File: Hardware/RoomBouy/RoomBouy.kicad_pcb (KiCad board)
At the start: 2 copper layers, 65 x 56.5 mm, 1 part, among them J2 Raspberry_Pi_2_3

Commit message: Clean sheet
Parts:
- moved J2 174.3 mm to (0.16, -24.8)
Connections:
- net Net-(J2-GND-Pad14) renamed GND
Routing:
- added copper zone on B.Cu, net GND
- added copper zone on F.Cu, net GND
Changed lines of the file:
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@@
 	(net 1 "unconnected-(J2-GPIO26-Pad37)")
 	(net 2 "Net-(J2-5V-Pad2)")
-	(net 3 "Net-(J2-GND-Pad14)")
+	(net 3 "GND")
 	(net 4 "unconnected-(J2-~{CE1}{slash}GPIO7-Pad26)")
 	(net 5 "unconnected-(J2-GPIO23-Pad16)")
@@
 	(footprint "RPI_Hat:RPI_Hat_B+"
 		(layer "F.Cu")
-		(at 144.24 73.222)
+		(at 0.16 -24.838)
 		(property "Reference" "J2"
 			(at 23.5 3.5 0)
@@
 			(layer "Dwgs.User")
 			(pts
-				(xy 115.24 126.722) (xy 111.74 126.722)
+				(xy -28.84 28.662) (xy -32.34 28.662)
 			)
 			(height -2.5)
 			(gr_text "3.5000 mm"
-				(at 113.49 127.572 0)
+				(at -30.59 29.512 0)
 				(layer "Dwgs.User")
 				(effects
@@
 			(layer "Dwgs.User")
 			(pts
-				(xy 158.74 122.722) (xy 158.74 105.722)
+				(xy 14.66 24.662) (xy 14.66 7.662)
 			)
 			(height 3)
 			(gr_text "17.0000 mm"
-				(at 160.09 114.222 90)
+				(at 16.01 16.162 90)
 				(layer "Dwgs.User")
 				(effects
@@
 			(layer "Dwgs.User")
 			(pts
-				(xy 154.74 125.722) (xy 154.74 114.222)
+				(xy 10.66 27.662) (xy 10.66 16.162)
 			)
 			(height -2.499999)
 			(gr_text "11.5000 mm"
-				(at 150.590001 119.972 90)
+				(at 6.510001 21.912 90)
 				(layer "Dwgs.User")
 				(effects
@@
 			(layer "Dwgs.User")
 			(pts
-				(xy 176.74 68.222) (xy 111.74 68.222)
+				(xy 32.66 -29.838) (xy -32.34 -29.838)
 			)
 			(height 7)
 			(gr_text "65.0000 mm"
-				(at 144.24 59.572 0)
+				(at 0.16 -38.488 0)
 				(layer "Dwgs.User")
 				(effects
@@
 			(layer "Dwgs.User")
 			(pts
-				(xy 110.74 125.722) (xy 110.74 106.222)
+				(xy -33.34 27.662) (xy -33.34 8.162)
 			)
 			(height -3)
 			(gr_text "19.5000 mm"
-				(at 106.09 115.972 90)
+				(at -37.99 17.912 90)
 				(layer "Dwgs.User")
 				(effects
@@
 			(layer "Dwgs.User")
 			(pts
-				(xy 177.74 125.722) (xy 177.74 69.722)
+				(xy 33.66 27.662) (xy 33.66 -28.338)
 			)
 			(height 8)
 			(gr_text "56.0000 mm"
-				(at 184.09 97.722 90)
+				(at 40.01 -0.338 90)
 				(layer "Dwgs.User")
 				(effects
@@
 			(layer "Dwgs.User")
 			(pts
-				(xy 157.74 104.722) (xy 155.74 104.722)
+				(xy 13.66 6.662) (xy 11.66 6.662)
 			)
 			(height 2.499999)
 			(gr_text "2.0000 mm"
-				(at 156.74 100.572001 0)
+				(at 12.66 2.512001 0)
 				(layer "Dwgs.User")
 				(effects
@@
 			(layer "Dwgs.User")
 			(pts
-				(xy 173.24 68.222) (xy 115.24 68.222)
+				(xy 29.16 -29.838) (xy -28.84 -29.838)
 			)
 			(height 2.5)
 			(gr_text "58.0000 mm"
-				(at 144.24 64.072 0)
+				(at 0.16 -33.988 0)
 				(layer "Dwgs.User")
 				(effects
@@
 			(layer "Dwgs.User")
 			(pts
-				(xy 177.74 122.222) (xy 177.74 73.222)
+				(xy 33.66 24.162) (xy 33.66 -24.838)
 			)
 			(height 2.999999)
 			(gr_text "49.0000 mm"
-				(at 179.089999 97.722 90)
+				(at 35.009999 -0.338 90)
 				(layer "Dwgs.User")
 				(effects
@@
 			(layer "Dwgs.User")
 			(pts
-				(xy 177.74 125.722) (xy 177.74 69.222)
+				(xy 33.66 27.662) (xy 33.66 -28.838)
 			)
 			(height 12)
 			(gr_text "56.5000 mm"
-				(at 188.09 97.472 90)
+				(at 44.01 -0.588 90)
 				(layer "Dwgs.User")
 				(effects
@@
 			(layer "Dwgs.User")
 			(pts
-				(xy 116.74 89.222) (xy 111.74 89.222)
+				(xy -27.34 -8.838) (xy -32.34 -8.838)
 			)
 			(height 2)
 			(gr_text "5.0000 mm"
-				(at 114.24 85.572 0)
+				(at -29.84 -12.488 0)
 				(layer "Dwgs.User")
 				(effects
@@
 			(layer "Dwgs.User")
 			(pts
-				(xy 118.74 125.722) (xy 118.74 122.222)
+				(xy -25.34 27.662) (xy -25.34 24.162)
 			)
 			(height 3)
 			(gr_text "3.5000 mm"
-				(at 120.09 123.972 90)
+				(at -23.99 25.912 90)
 				(layer "Dwgs.User")
 				(effects
@@
 			(layer "Dwgs.User")
 			(pts
-				(xy 144.24 75.222001) (xy 115.24 75.222001)
+				(xy 0.16 -22.837999) (xy -28.84 -22.837999)
 			)
 			(height -2.499999)
 			(gr_text "29.0000 mm"
-				(at 129.74 79.722001 0)
+				(at -14.34 -18.337999 0)
 				(layer "Dwgs.User")
 				(effects
@@
 			(layer "Dwgs.User")
 			(pts
-				(xy 117.74 106.222) (xy 117.74 89.222)
+				(xy -26.34 8.162) (xy -26.34 -8.838)
 			)
 			(height 2)
 			(gr_text "17.0000 mm"
-				(at 118.09 97.722 90)
+				(at -25.99 -0.338 90)
 				(layer "Dwgs.User")
 				(effects
@@
 			(layers "*.Cu" "*.Mask")
 			(remove_unused_layers no)
-			(net 3 "Net-(J2-GND-Pad14)")
+			(net 3 "GND")
 			(pinfunction "GND")
 			(pintype "power_in")
@@
 			(layers "*.Cu" "*.Mask")
 			(remove_unused_layers no)
-			(net 3 "Net-(J2-GND-Pad14)")
+			(net 3 "GND")
 			(pinfunction "GND")
 			(pintype "passive")
@@
 			(layers "*.Cu" "*.Mask")
 			(remove_unused_layers no)
-			(net 3 "Net-(J2-GND-Pad14)")
+			(net 3 "GND")
 			(pinfunction "GND")
 			(pintype "passive")
@@
 			(layers "*.Cu" "*.Mask")
 			(remove_unused_layers no)
-			(net 3 "Net-(J2-GND-Pad14)")
+			(net 3 "GND")
 			(pinfunction "GND")
 			(pintype "passive")
@@
 			(layers "*.Cu" "*.Mask")
 			(remove_unused_layers no)
-			(net 3 "Net-(J2-GND-Pad14)")
+			(net 3 "GND")
 			(pinfunction "GND")
 			(pintype "passive")
@@
 			(layers "*.Cu" "*.Mask")
 			(remove_unused_layers no)
-			(net 3 "Net-(J2-GND-Pad14)")
+			(net 3 "GND")
 			(pinfunction "GND")
 			(pintype "passive")
@@
 			(layers "*.Cu" "*.Mask")
 			(remove_unused_layers no)
-			(net 3 "Net-(J2-GND-Pad14)")
+			(net 3 "GND")
 			(pinfunction "GND")
 			(pintype "passive")
@@
 			(layers "*.Cu" "*.Mask")
 			(remove_unused_layers no)
-			(net 3 "Net-(J2-GND-Pad14)")
+			(net 3 "GND")
 			(pinfunction "GND")
 			(pintype "passive")
@@
 		)
 	)
+	(zone
+		(net 3)
+		(net_name "GND")
+		(layers "F&B.Cu")
+		(hatch edge 0.5)
+		(connect_pads
+			(clearance 0.5)
+		)
+		(min_thickness 0.25)
+		(filled_areas_thickness no)
+		(fill yes
+			(thermal_gap 0.5)
+			(thermal_bridge_width 0.5)
+		)
+		(polygon
+			(pts
+				(xy 32.92 -29.06) (xy 32.92 27.94) (xy -33.08 27.94) (xy -33.08 -29.06)
+			)
+		)
+	)

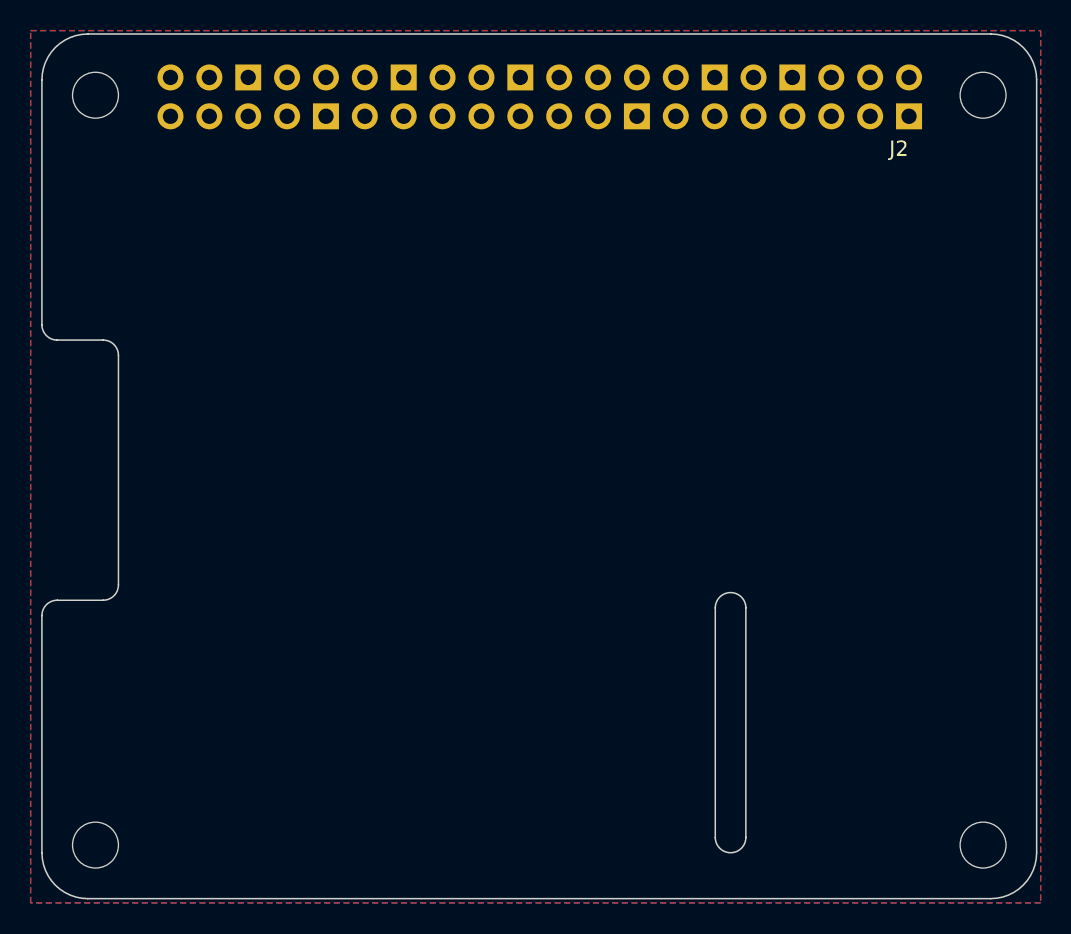
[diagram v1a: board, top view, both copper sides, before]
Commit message: Add internal libs, do full board layout, bump k8 and fix ERC
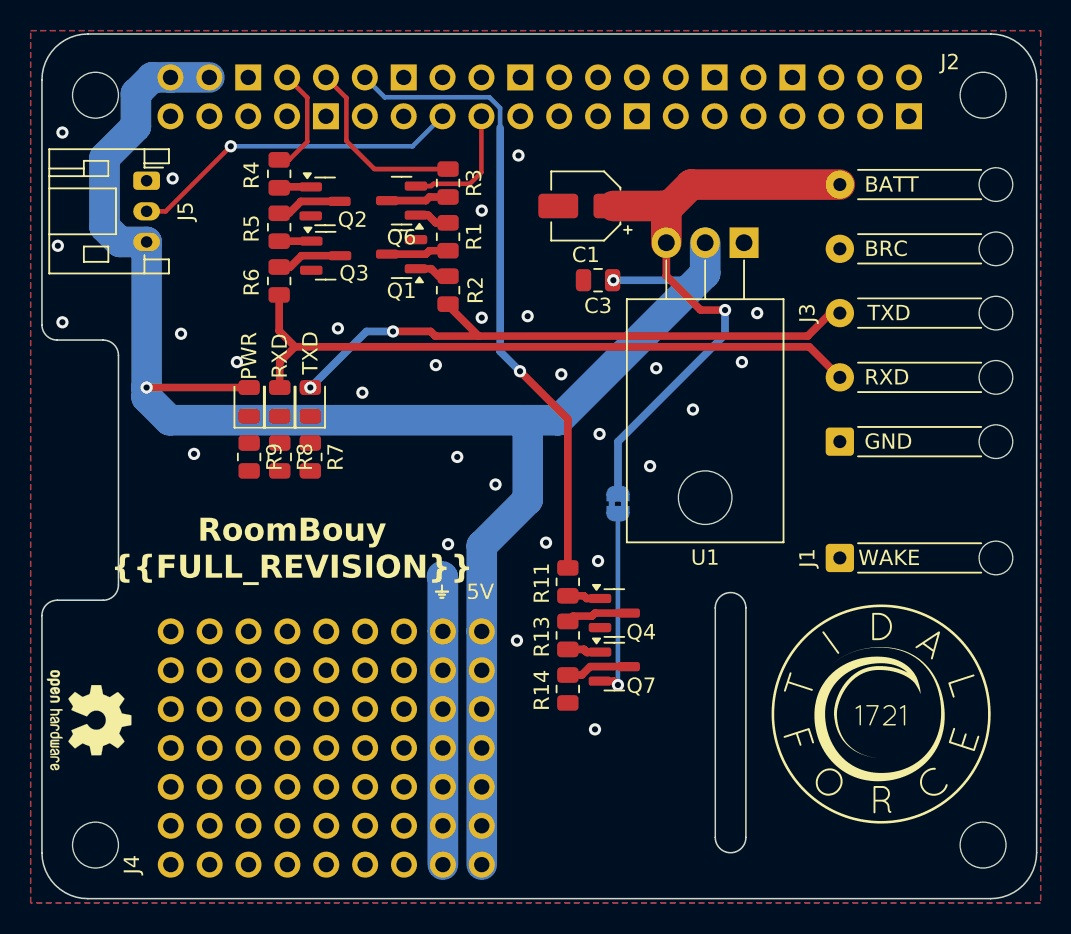
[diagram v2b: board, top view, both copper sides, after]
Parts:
- added C1: 10uf, Capacitor_SMD:CP_Elec_4x3, F.Cu at (3.20, -17.6)
- added C3: 1uF, Capacitor_SMD:C_0805_2012Metric, F.Cu at (4.00, -12.8)
- added D1: TXD, LED_SMD:LED_0805_2012Metric, F.Cu at (-14.8, -4.80)
- added D2: RXD, LED_SMD:LED_0805_2012Metric, F.Cu at (-16.8, -4.80)
- added D3: PWR, LED_SMD:LED_0805_2012Metric, F.Cu at (-18.8, -4.80)
- added G***: LOGO, KenwoodFox:TIDAL_FORCE_LOGO, F.Cu at (22.5, 15.6)
- added G***: LOGO, KenwoodFox:KITSUNE_LOGO, B.Cu at (21.0, 15.8)
- added J1: Roomba Wake, Connector_Wire:SolderWire-0.25sqmm_1x01_D0.65mm_OD1.7mm_Relief, F.Cu at (19.8, 5.40)
- added J3: Roomba Connector, Connector_Wire:SolderWire-0.25sqmm_1x05_P4.2mm_D0.65mm_OD1.7mm_Relief, F.Cu at (19.8, -2.20)
- added J4: ProtoPad, RoomBouy:ProtoPad, F.Cu at (-13.8, 17.8)
- added J5: Servo, Connector_JST:JST_PH_S3B-PH-K_1x03_P2.00mm_Horizontal, F.Cu at (-25.5, -19.2)
- added JP1: SolderJumper_2_Bridged, Jumper:SolderJumper-2_P1.3mm_Bridged2Bar_RoundedPad1.0x1.5mm, B.Cu at (5.30, 1.85)
- added Q1: MMBT3904, Package_TO_SOT_SMD:SOT-23, F.Cu at (-8.84, -14.4)
- added Q2: MMBT3904, Package_TO_SOT_SMD:SOT-23, F.Cu at (-13.8, -17.9)
- added Q3: MMBT3906, Package_TO_SOT_SMD:SOT-23, F.Cu at (-13.8, -14.3)
- added Q4: MMBT3904, Package_TO_SOT_SMD:SOT-23, F.Cu at (5.06, 9.00)
- added Q6: MMBT3906, Package_TO_SOT_SMD:SOT-23, F.Cu at (-8.84, -17.9)
- added Q7: MMBT3906, Package_TO_SOT_SMD:SOT-23, F.Cu at (5.06, 12.5)
- added R1: 1k, Resistor_SMD:R_0805_2012Metric, F.Cu at (-5.80, -15.6)
- added R11: 1k, Resistor_SMD:R_0805_2012Metric, F.Cu at (2.02, 6.96)
- added R13: 1k, Resistor_SMD:R_0805_2012Metric, F.Cu at (2.02, 10.5)
- added R14: 1k, Resistor_SMD:R_0805_2012Metric, F.Cu at (2.02, 14.0)
- added R2: 1k, Resistor_SMD:R_0805_2012Metric, F.Cu at (-5.80, -12.1)
- added R3: 1k, Resistor_SMD:R_0805_2012Metric, F.Cu at (-5.80, -19.1)
- added R4: 1k, Resistor_SMD:R_0805_2012Metric, F.Cu at (-16.8, -19.7)
- added R5: 1k, Resistor_SMD:R_0805_2012Metric, F.Cu at (-16.8, -16.2)
- added R6: 1k, Resistor_SMD:R_0805_2012Metric, F.Cu at (-16.8, -12.7)
- added R7: 1k, Resistor_SMD:R_0805_2012Metric, F.Cu at (-14.8, -1.20)
- added R8: 1k, Resistor_SMD:R_0805_2012Metric, F.Cu at (-16.8, -1.20)
- added R9: 1k, Resistor_SMD:R_0805_2012Metric, F.Cu at (-18.8, -1.20)
- added REF**: OSHW-Logo2_7.3x6mm_SilkScreen, Symbol:OSHW-Logo2_7.3x6mm_SilkScreen, F.Cu at (-29.2, 16.0)
- added REF**: KiCad-Logo2_5mm_SilkScreen, Symbol:KiCad-Logo2_5mm_SilkScreen, B.Cu at (20.8, 23.8)
- added U1: LM1084-5.0, Package_TO_SOT_THT:TO-220-3_Horizontal_TabDown, F.Cu at (13.5, -15.2)
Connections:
- net Net-(J2-3V3-Pad1) renamed +3.3V
- net Net-(J2-5V-Pad2) renamed +5V
- J2 pad 10: unconnected-(J2-GPIO15/RXD-Pad10) -> /PI_RXD
- J2 pad 12: unconnected-(J2-GPIO18/PWM0-Pad12) -> /GPIO18
- J2 pad 15: unconnected-(J2-GPIO22-Pad15) -> /SERVO
- J2 pad 8: unconnected-(J2-GPIO14/TXD-Pad8) -> /PI_TXD
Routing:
- net +5V: track 0.00 -> 114.4 mm, vias 0 -> 2
- net /ROOMBA_RXD: track 0.00 -> 43.3 mm
- net /GPIO18: track 0.00 -> 41.6 mm, vias 0 -> 1
- net /ROOMBA_TXD: track 0.00 -> 39.8 mm, vias 0 -> 2
- net +BATT: track 0.00 -> 39.6 mm, vias 0 -> 1
- net /SERVO: track 0.00 -> 21.9 mm, vias 0 -> 1
- net GND: track 0.00 -> 18.9 mm, vias 0 -> 28
- net Net-(JP1-A): track 0.00 -> 12.5 mm, vias 0 -> 1
- net /PI_RXD: track 0.00 -> 12.1 mm
- net +3.3V: track 0.00 -> 8.31 mm
- net /PI_TXD: track 0.00 -> 7.08 mm
- net Net-(Q3-C): track 0.00 -> 4.28 mm
- net Net-(Q2-C): track 0.00 -> 4.26 mm
- net Net-(Q7-C): track 0.00 -> 4.20 mm
- net Net-(Q4-C): track 0.00 -> 4.20 mm
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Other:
- board text added: "5V"
- board text added: "BATT"
- board text added: "BRC"
- board text added: "GND"
- board text added: "RXD"
- board text added: "RoomBouy {{FULL_REVISION}}"
- board text added: "TXD"
- board text added: "WAKE"
- board text added: "{dblquote}Societies get the best of what they celebrate.{dblquote} -Woodie Flowers"

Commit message: Fix DRC
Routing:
- net /ROOMBA_WAKE: track 0.00 -> 23.7 mm
- net +5V: track 114.4 -> 125.5 mm, vias 2 -> 3
- net Net-(D3-K): track 0.00 -> 1.75 mm
- net Net-(D2-K): track 0.00 -> 1.75 mm
- net Net-(D1-K): track 0.00 -> 1.75 mm
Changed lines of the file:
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@@
 		(tags "SOT TO_SOT_SMD")
 		(property "Reference" "Q4"
-			(at 1.7625 1.25 360)
+			(at 1.7625 1.25 0)
 			(layer "F.SilkS")
 			(effects
@@
 		)
 		(property "Value" "MMBT3904"
-			(at 0 2.4 360)
+			(at 0 2.4 0)
 			(layer "F.Fab")
 			(effects
@@
 		)
 		(fp_text user "${REFERENCE}"
-			(at 0 0 360)
+			(at 0 0 0)
 			(layer "F.Fab")
 			(effects
@@
 		(tags "resistor")
 		(property "Reference" "R8"
-			(at 0 -1.65 90)
+			(at 2.7 -0.05 90)
 			(layer "F.SilkS")
 			(effects
@@
 		(tags "SOT TO_SOT_SMD")
 		(property "Reference" "Q2"
-			(at 1.8 1.2 360)
+			(at 1.8 1.2 0)
 			(layer "F.SilkS")
 			(effects
@@
 		)
 		(property "Value" "MMBT3904"
-			(at 0 2.4 360)
+			(at 0 2.4 0)
 			(layer "F.Fab")
 			(effects
@@
 		)
 		(fp_text user "${REFERENCE}"
-			(at 0 0 360)
+			(at 0 0 0)
 			(layer "F.Fab")
 			(effects
@@
 		(tags "capacitor electrolytic")
 		(property "Reference" "C1"
-			(at 0 -3.2 360)
+			(at 0 -3.2 0)
 			(layer "F.SilkS")
 			(effects
@@
 		)
 		(property "Value" "10uf"
-			(at 0 3.2 360)
+			(at 0 3.2 0)
 			(layer "F.Fab")
 			(effects
@@
 		)
 		(fp_text user "${REFERENCE}"
-			(at 0 0 360)
+			(at 0 0 0)
 			(layer "F.Fab")
 			(effects
@@
 		(tags "TO-220-3 Horizontal RM 2.54mm")
 		(property "Reference" "U1"
-			(at 2.54 -20.58 360)
+			(at 2.54 -20.58 0)
 			(layer "F.SilkS")
 			(effects
@@
 		)
 		(property "Value" "LM1084-5.0"
-			(at 2.54 2 360)
+			(at 2.54 2 0)
 			(layer "F.Fab")
 			(effects
@@
 		)
 		(fp_text user "${REFERENCE}"
-			(at 2.54 -20.58 360)
+			(at 2.54 -20.58 0)
 			(layer "F.Fab")
 			(effects
@@
 		(tags "capacitor")
 		(property "Reference" "C3"
-			(at 0 -1.68 360)
+			(at 0 -1.68 0)
 			(layer "F.SilkS")
 			(effects
@@
 		)
 		(property "Value" "1uF"
-			(at 0 1.68 360)
+			(at 0 1.68 0)
 			(layer "F.Fab")
 			(effects
@@
 		)
 		(fp_text user "${REFERENCE}"
-			(at 0 0 360)
+			(at 0 0 0)
 			(layer "F.Fab")
 			(effects
@@
 		(tags "resistor")
 		(property "Reference" "R9"
-			(at 0 -1.65 90)
+			(at 2.7 -0.05 90)
 			(layer "F.SilkS")
 			(effects
@@
 		(tags "resistor")
 		(property "Reference" "R7"
-			(at 0 -1.65 90)
+			(at 2.7 -0.05 90)
 			(layer "F.SilkS")
 			(effects
@@
 		(tags "SOT TO_SOT_SMD")
 		(property "Reference" "Q6"
-			(at 0 -2.4 360)
+			(at 0 -2.4 0)
 			(layer "F.SilkS")
 			(effects
@@
 		)
 		(property "Value" "MMBT3906"
-			(at 0 2.4 360)
+			(at 0 2.4 0)
 			(layer "F.Fab")
 			(effects
@@
 		)
 		(fp_text user "${REFERENCE}"
-			(at 0 0 360)
+			(at 0 0 0)
 			(layer "F.Fab")
 			(effects
@@
 		)
 		(fp_text user "${REFERENCE}"
-			(at 8.4 5.1 360)
+			(at 8.4 5.1 0)
 			(layer "F.Fab")
 			(effects
@@
 		(tags "SOT TO_SOT_SMD")
 		(property "Reference" "Q1"
-			(at 0 -2.4 360)
+			(at 0 -2.4 0)
 			(layer "F.SilkS")
 			(effects
@@
 		)
 		(property "Value" "MMBT3904"
-			(at 0 2.4 360)
+			(at 0 2.4 0)
 			(layer "F.Fab")
 			(effects
@@
 		)
 		(fp_text user "${REFERENCE}"
-			(at 0 0 360)
+			(at 0 0 0)
 			(layer "F.Fab")
 			(effects
@@
 		(at 21 15.75 180)
 		(property "Reference" "G***"
-			(at 0 0 360)
+			(at 0 0 0)
 			(layer "B.SilkS")
 			(hide yes)
@@
 		)
 		(property "Value" "LOGO"
-			(at 0.75 0 360)
+			(at 0.75 0 0)
 			(layer "B.SilkS")
 			(hide yes)
@@
 	)
 	(segment
+		(start 19.8 5.4)
+		(end 13.85 5.4)
+		(width 0.5)
+		(layer "F.Cu")
+		(net 30)
+	)
+	(segment
+		(start 10.25 9)
+		(end 10.25 12.5)
+		(width 0.5)
+		(layer "F.Cu")
+		(net 30)
+	)
+	(segment
+		(start 13.85 5.4)
+		(end 10.25 9)
+		(width 0.5)
+		(layer "F.Cu")
+		(net 30)
+	)
+	(segment
+		(start 10.25 12.5)
+		(end 7.875 14.875)
+		(width 0.5)
+		(layer "F.Cu")
+		(net 30)
+	)
+	(segment
+		(start 7.875 14.875)
+		(end 2.025 14.875)
+		(width 0.5)
+		(layer "F.Cu")
+		(net 30)
+	)
+	(segment
 		(start 4.95 -12.75)
 		(end 5 -12.75)
@@
 		(net 31)
 	)
+	(segment
+		(start -14.7375 -13.4)
+		(end -15.3875 -12.75)
+		(width 0.3)
+		(layer "F.Cu")
+		(net 31)
+	)
+	(segment
+		(start -15.3875 -12.75)
+		(end -25.25 -12.75)
+		(width 0.3)
+		(layer "F.Cu")
+		(net 31)
+	)
+	(segment
+		(start -25.25 -12.75)
+		(end -25.5 -12.5)
+		(width 0.3)
+		(layer "F.Cu")
+		(net 31)
+	)
 	(via
 		(at -25.5 -5.7375)
@@
 		(net 31)
 	)
+	(via
+		(at -25.5 -12.5)
+		(size 0.8)
+		(drill 0.4)
+		(layers "F.Cu" "B.Cu")
+		(net 31)
+	)
+	(segment
+		(start -25.5 -5.7375)
+		(end -25.5 -12.5)
+		(width 2)
+		(layer "B.Cu")
+		(net 31)
+	)
 	(segment
 		(start -28.25 -16.25)
@@
 	)
 	(segment
+		(start -25.5 -12.5)
+		(end -25.5 -15.25)
+		(width 2)
+		(layer "B.Cu")
+		(net 31)
+	)
+	(segment
 		(start -23.94 -26)
 		(end -25.142081 -26)
@@
 	)
 	(segment
-		(start -25.5 -5.7375)
-		(end -25.5 -15.25)
-		(width 2)
-		(layer "B.Cu")
-		(net 31)
-	)
-	(segment
 		(start 11 -13.2)
 		(end 1.4 -3.6)
@@
 	)
 	(segment
+		(start -14.8 -3.8625)
+		(end -14.8 -2.1125)
+		(width 0.5)
+		(layer "F.Cu")
+		(net 41)
+	)
+	(segment
+		(start -16.8 -3.8625)
+		(end -16.8 -2.1125)
+		(width 0.5)
+		(layer "F.Cu")
+		(net 42)
+	)
+	(segment
+		(start -18.8 -3.8625)
+		(end -18.8 -2.1125)
+		(width 0.5)
+		(layer "F.Cu")
+		(net 43)
+	)
+	(segment

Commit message: Fix revision tag
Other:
- board text added: "RoomBouy ${FULL_REVISION}"
- board text removed: "RoomBouy {{FULL_REVISION}}"
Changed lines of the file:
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@@
 		)
 	)
-	(gr_text "RoomBouy\n{{FULL_REVISION}}"
+	(gr_text "RoomBouy\n${FULL_REVISION}"
 		(at -16 2.7 0)
 		(layer "F.SilkS")
